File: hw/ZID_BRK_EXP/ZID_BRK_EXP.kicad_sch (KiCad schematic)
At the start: 33 parts, among them J1 BRK-EXP-UNIT, J2 Conn_02x05_PINHDR_2.54mm, U1 ATF1504AS-44T, U2 ATF1504AS-44T

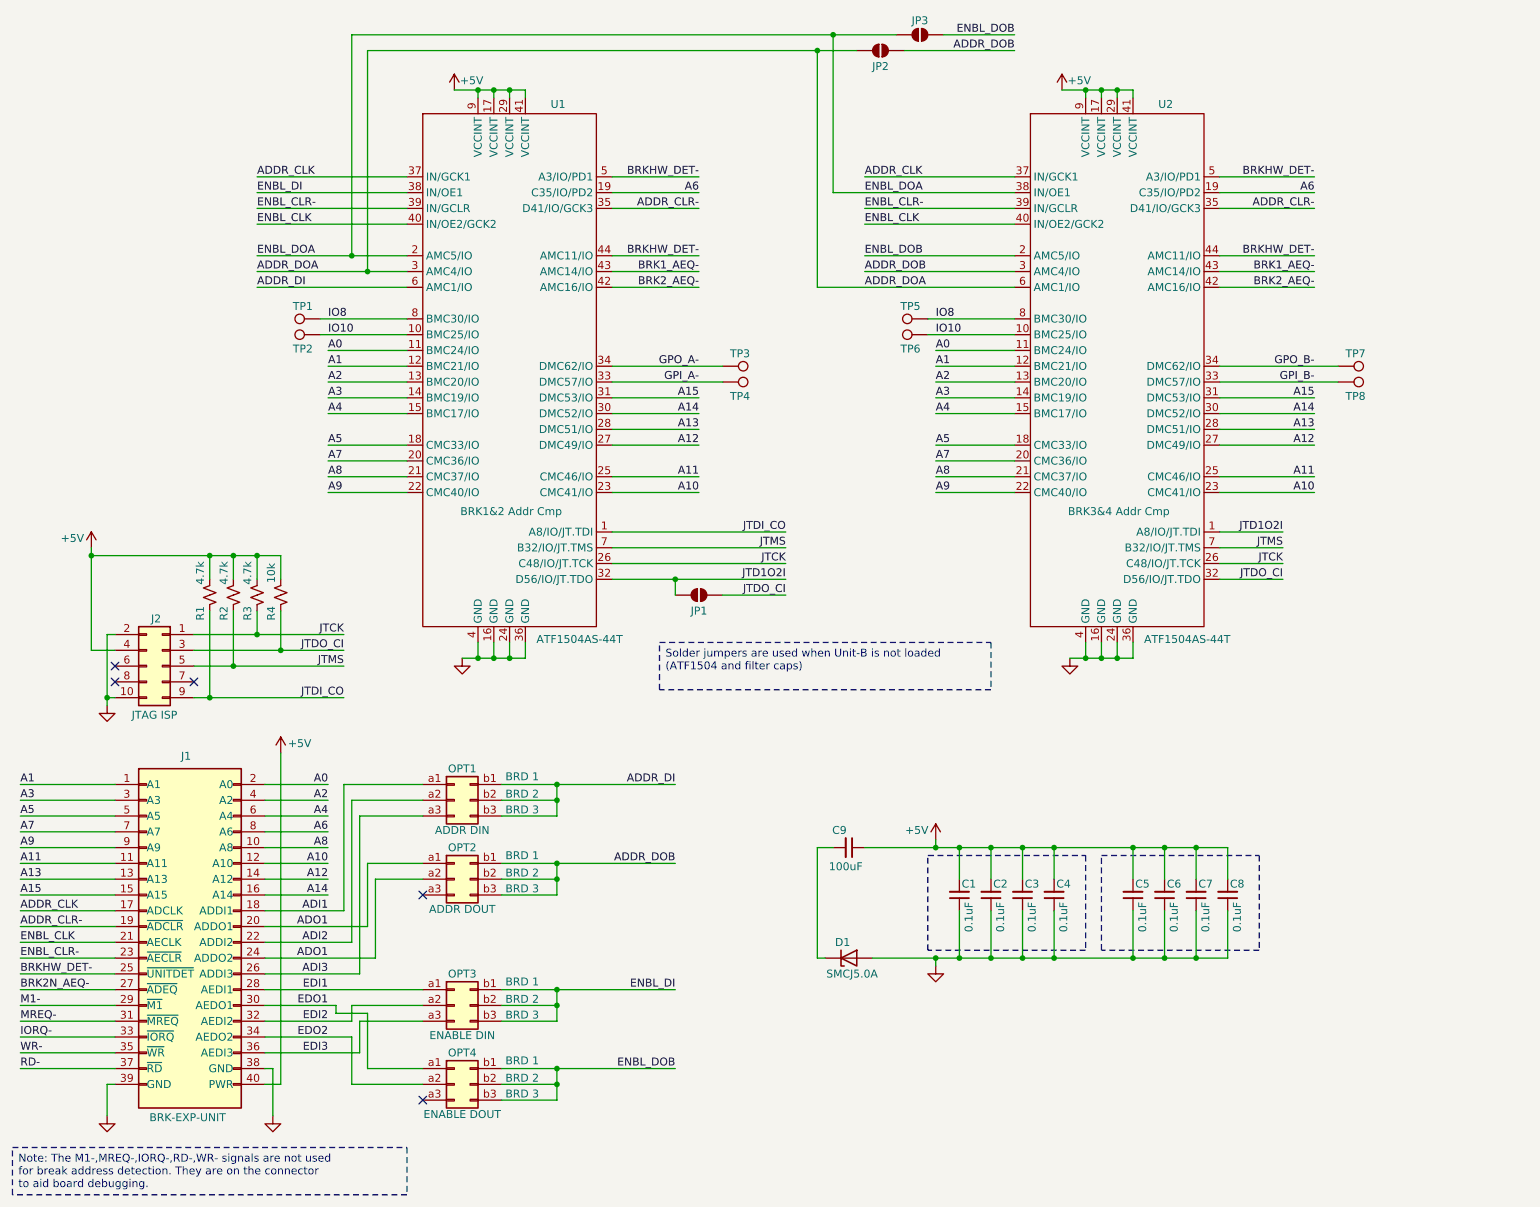
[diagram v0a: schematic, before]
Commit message: BP-EXP: 1 board only. PLCC-DIP: Adapter form.
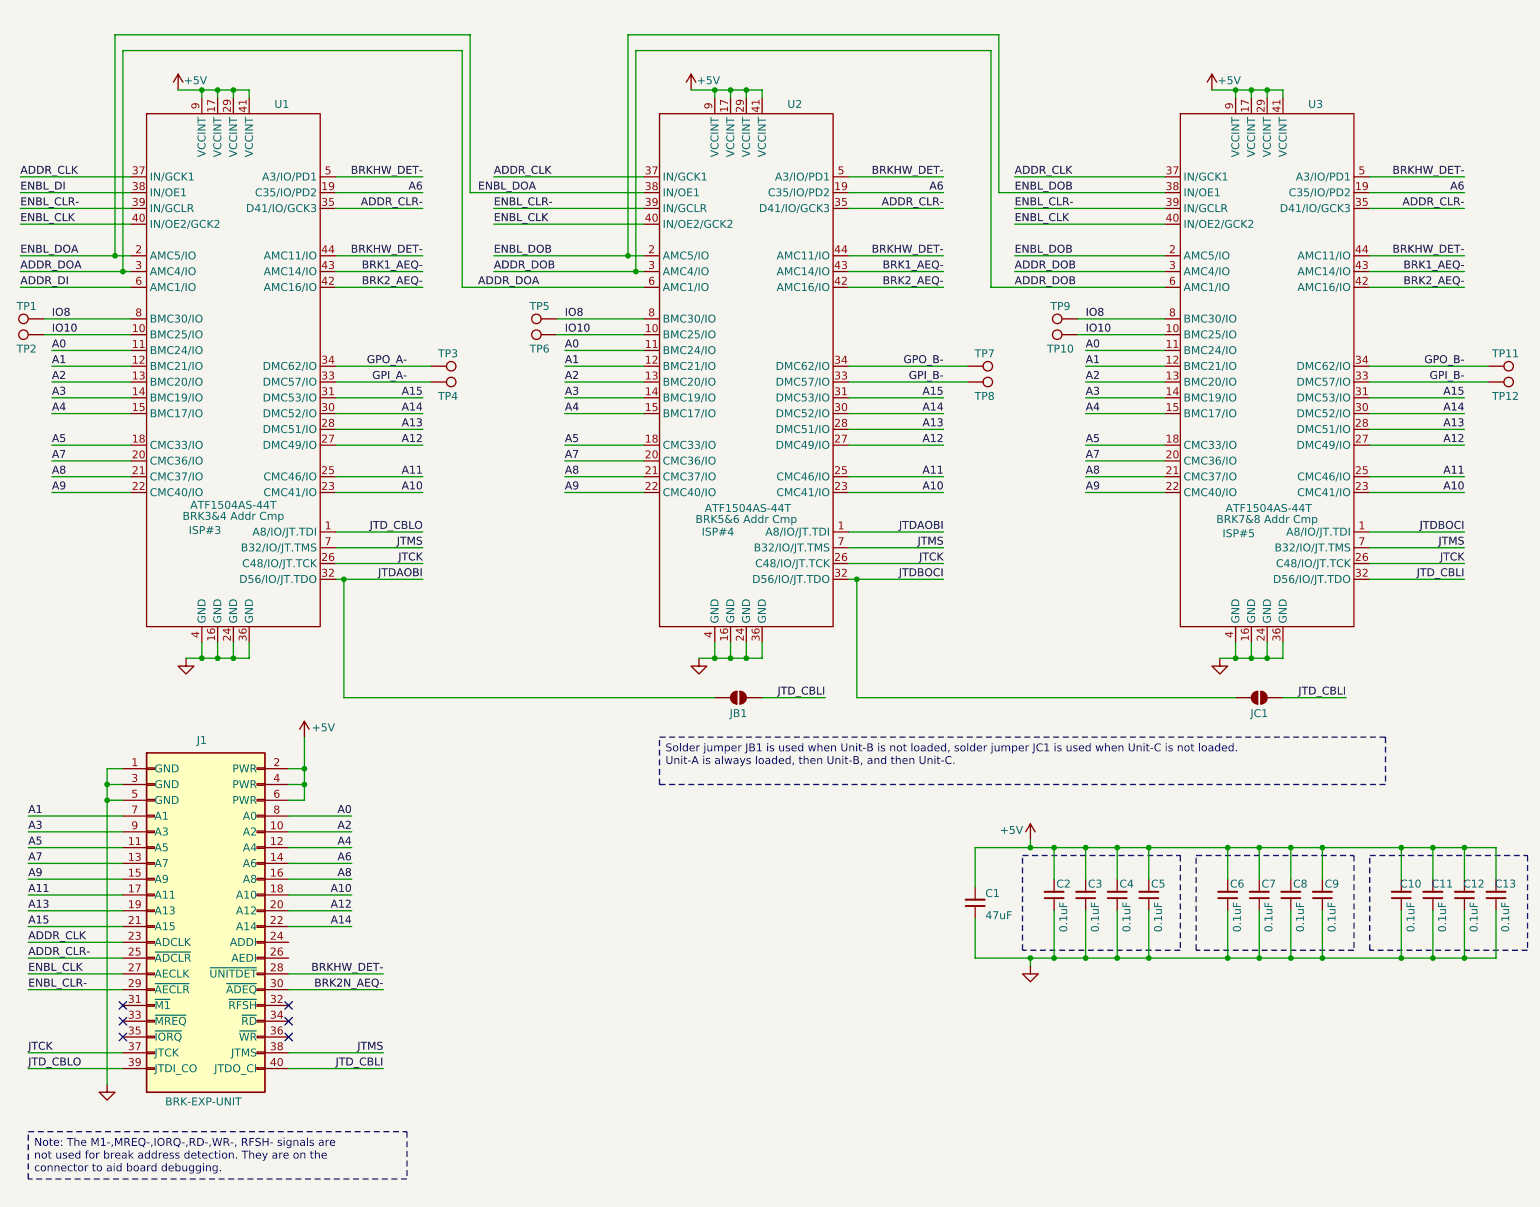
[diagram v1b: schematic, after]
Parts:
- removed D1: SMCJ5.0A, Diode_SMD:D_SOD-523, symbol Diode:ESD5Zxx
- removed J2: Conn_02x05_PINHDR_2.54mm, Connector_IDC:IDC-Header_2x05_P2.54mm_Vertical, symbol Connector_Generic:Conn_02x05_Odd_Even
- removed JP2, JP3: SolderJumper_2_Open, symbol Jumper:SolderJumper_2_Open
- removed OPT1, OPT2, OPT3, OPT4: Conn_02x03_Row_Letter_First, symbol Connector_Generic:Conn_02x03_Row_Letter_First
- removed R1, R2, R3: 4.7k, Resistor_SMD:R_0805_2012Metric, symbol Device:R_Small_US
- removed R4: 10k, Resistor_SMD:R_0805_2012Metric, symbol Device:R_Small_US
- added C10, C11, C12, C13: 0.1uF, Capacitor_SMD:C_0603_1608Metric, symbol Device:C_Small
- added JC1: SolderJumper_2_Open, symbol Jumper:SolderJumper_2_Open
- added TP10, TP11, TP12, TP9: TestPoint, Connector_PinHeader_2.54mm:PinHeader_1x01_P2.54mm_Vertical, symbol Connector:TestPoint
- added U3: ATF1504AS-44T, Package_QFP:TQFP-44_10x10mm_P0.8mm, symbol AES_Library:ATF1504AS-44T-AES
- C1: renamed from C9; value 100uF -> 47uF
- J1: JTAG_NOTE1 (none) -> SHORT 39-40; JTAG_NOTE2 (none) -> for JTAG-ISP
- U1: Function BRK1&2 Addr Cmp -> BRK3&4 Addr Cmp; ISP_CN (none) -> ISP#3
- U2: Function BRK3&4 Addr Cmp -> BRK5&6 Addr Cmp; ISP_CN (none) -> ISP#4
- renumbered C1 to C2, C2 to C3, C3 to C4, C4 to C5, C5 to C6, C6 to C7, C7 to C8, C8 to C9, JP1 to JB1
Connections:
- net ADI1 is gone; now on net A10: J1.18 (A10)
- net ADI2 is gone; now on net A14: J1.22 (A14)
- net EDI1 is gone; now on net BRKHW_DET-: J1.28 (~{UNITDET})
- net EDO1 is gone; now on net BRK2N_AEQ-: J1.30 (~{ADEQ})
- net M1- is gone; now on net ENBL_CLR-: J1.29 (~{AECLR})
- net RD- is gone; now on net JTCK: J1.37 (JTCK)
- net +5V: now also C1.2, J1.2 (PWR), J1.4 (PWR), J1.6 (PWR), C10.2, C11.2, C12.2, C13.2, U3.17 (VCCINT), U3.29 (VCCINT), U3.41 (VCCINT), U3.9 (VCCINT); no longer C1.1, J1.40 (PWR)
- net A0: now also J1.8 (A0), U3.11 (BMC24/IO); no longer J1.2 (A0)
- net A1: now also J1.7 (A1), U3.12 (BMC21/IO); no longer J1.1 (A1)
- net A10: now also U3.23 (CMC41/IO); no longer J1.12 (A10)
- net A11: now also J1.17 (A11), U3.25 (CMC46/IO); no longer J1.11 (A11)
- net A12: now also J1.20 (A12), U3.27 (DMC49/IO); no longer J1.14 (A12)
- net A13: now also J1.19 (A13), U3.28 (DMC51/IO); no longer J1.13 (A13)
- net A14: now also U3.30 (DMC52/IO); no longer J1.16 (A14)
- net A15: now also J1.21 (A15), U3.31 (DMC53/IO); no longer J1.15 (A15)
- net A2: now also J1.10 (A2), U3.13 (BMC20/IO); no longer J1.4 (A2)
- net A3: now also J1.9 (A3), U3.14 (BMC19/IO); no longer J1.3 (A3)
- net A4: now also J1.12 (A4), U3.15 (BMC17/IO); no longer J1.6 (A4)
- net A5: now also J1.11 (A5), U3.18 (CMC33/IO); no longer J1.5 (A5)
- net A6: now also J1.14 (A6), U3.19 (C35/IO/PD2); no longer J1.8 (A6)
- net A7: now also J1.13 (A7), U3.20 (CMC36/IO); no longer J1.7 (A7)
- net A8: now also J1.16 (A8), U3.21 (CMC37/IO); no longer J1.10 (A8)
- net A9: now also J1.15 (A9), U3.22 (CMC40/IO); no longer J1.9 (A9)
- net ADDR_CLK: now also J1.23 (ADCLK), U3.37 (IN/GCK1); no longer J1.17 (ADCLK)
- net ADDR_CLR-: now also J1.25 (~{ADCLR}), U3.35 (D41/IO/GCK3); no longer J1.19 (~{ADCLR})
- net ADDR_DOB: now also U3.3 (AMC4/IO), U3.6 (AMC1/IO)
- net BRK1_AEQ-: now also U3.43 (AMC14/IO)
- net BRK2N_AEQ-: no longer J1.27 (~{ADEQ})
- net BRK2_AEQ-: now also U3.42 (AMC16/IO)
- net BRKHW_DET-: now also U3.44 (AMC11/IO), U3.5 (A3/IO/PD1); no longer J1.25 (~{UNITDET})
- net ENBL_CLK: now also J1.27 (AECLK), U3.40 (IN/OE2/GCK2); no longer J1.21 (AECLK)
- net ENBL_CLR-: now also U3.39 (IN/GCLR); no longer J1.23 (~{AECLR})
- net ENBL_DOB: now also U3.2 (AMC5/IO), U3.38 (IN/OE1)
- net GND: now also C1.1, J1.1 (GND), J1.3 (GND), J1.5 (GND), C10.1, C11.1, C12.1, C13.1, U3.16 (GND), U3.24 (GND), U3.36 (GND), U3.4 (GND); no longer J1.38 (GND), J1.39 (GND)
- net GPI_B-: now also TP12.1, U3.33 (DMC57/IO)
- net GPO_B-: now also TP11.1, U3.34 (DMC62/IO)
- net IO10: now also TP10.1, U3.10 (BMC25/IO)
- net IO8: now also TP9.1, U3.8 (BMC30/IO)
- net JTCK: now also U3.26 (C48/IO/JT.TCK)
- net JTMS: now also J1.38 (JTMS), U3.7 (B32/IO/JT.TMS)
- net ADI3: no longer names the net of J1.26 (AEDI)
- net ADO1: no longer names the net of J1.24 (ADDI)
- net ADO1: no longer J1.20 (ADDO1)
- net EDI2: no longer names the net of J1.32 (~{RFSH})
- net EDI3: no longer names the net of J1.36 (~{WR})
- net EDO2: no longer names the net of J1.34 (~{RD})
- net IORQ-: no longer names the net of J1.33 (~{MREQ})
- net JTD1O2I renamed JTDAOBI
- net JTDI_CO renamed JTD_CBLO
- net JTD_CBLO: now also J1.39 (JTDI_CO)
- net JTDO_CI renamed JTDBOCI
- net JTDBOCI: now also JC1.1 (A), U3.1 (A8/IO/JT.TDI); no longer JB1.2 (B)
- net MREQ-: no longer names the net of J1.31 (~{M1})
- net WR-: no longer names the net of J1.35 (~{IORQ})
- new net JTD_CBLI: J1.40 (JTDO_CI), JB1.2 (B), JC1.2 (B), U3.32 (D56/IO/JT.TDO)
- no-connect marks 5 -> 6
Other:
- moved on the sheet: C1, C2, C3, C4, C5, C6, C7, C8, C9, J1, JB1, TP1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
